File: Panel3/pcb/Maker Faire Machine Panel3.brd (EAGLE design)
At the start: 101.6 x 87.6 mm, 22 parts, among them IC1 TJA1049

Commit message: Add 2nd CAN terminal block for ease of wiring
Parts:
- added JP8: (no value), SparkFun-Connectors:SCREWTERMINAL-3.5MM-2
- renumbered JP3 to JP9
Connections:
- net CANH: now also JP8.1
- net CANL: now also JP8.2
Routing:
- net CANL: track 16.5 -> 27.3 mm
- net CANH: track 17.7 -> 28.0 mm
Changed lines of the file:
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@@
 <attribute name="PARTNO" value="12065C104KAT2A" x="62.23" y="12.7" size="1.778" layer="27" display="off"/>
 </element>
-<element name="JP3" library="SparkFun-Connectors" package="SCREWTERMINAL-3.5MM-2" value="" x="92.71" y="26.67" rot="R90">
+<element name="JP9" library="SparkFun-Connectors" package="SCREWTERMINAL-3.5MM-2" value="" x="92.71" y="26.67" rot="R90">
 <attribute name="PROD_ID" value="CONN-08399" x="92.71" y="26.67" size="1.778" layer="27" rot="R90" display="off"/>
 </element>
@@
 <element name="JP7" library="SparkFun-Connectors" package="POWER_JACK_PTH" value="POWER_JACKPTH" x="13.97" y="87.63" rot="R180">
 <attribute name="PROD_ID" value="CONN-08197" x="13.97" y="87.63" size="1.778" layer="27" rot="R180" display="off"/>
+</element>
+<element name="JP8" library="SparkFun-Connectors" package="SCREWTERMINAL-3.5MM-2" value="" x="92.71" y="16.51" rot="R90">
+<attribute name="PROD_ID" value="CONN-08399" x="92.71" y="16.51" size="1.778" layer="27" rot="R90" display="off"/>
 </element>
 </elements>
@@
 <vertex x="1.27" y="7.62"/>
 </polygon>
+<wire x1="82.61" y1="28.575" x2="77.41" y2="27.305" width="0" layer="19" extent="1-1"/>
 </signal>
 <signal name="VBAT">
@@
 <signal name="CANH">
 <contactref element="IC1" pad="7"/>
-<contactref element="JP3" pad="1"/>
+<contactref element="JP9" pad="1"/>
 <wire x1="79.375" y1="28.575" x2="77.41" y2="28.575" width="0.254" layer="1"/>
 <wire x1="79.375" y1="27.305" x2="79.375" y2="28.575" width="0.254" layer="1"/>
 <wire x1="80.645" y1="26.035" x2="79.375" y2="27.305" width="0.254" layer="1"/>
-<wire x1="92.71" y1="26.035" x2="80.645" y2="26.035" width="0.254" layer="1"/>
+<wire x1="92.71" y1="26.035" x2="90.805" y2="26.035" width="0.254" layer="1"/>
+<wire x1="90.805" y1="26.035" x2="80.645" y2="26.035" width="0.254" layer="1"/>
 <wire x1="92.71" y1="26.67" x2="92.71" y2="26.035" width="0.254" layer="1"/>
+<contactref element="JP8" pad="1"/>
+<wire x1="90.805" y1="18.415" x2="92.71" y2="16.51" width="0.254" layer="1"/>
+<wire x1="90.805" y1="26.035" x2="90.805" y2="18.415" width="0.254" layer="1"/>
 </signal>
 <signal name="CANL">
 <contactref element="IC1" pad="6"/>
-<contactref element="JP3" pad="2"/>
+<contactref element="JP9" pad="2"/>
 <wire x1="80.645" y1="29.845" x2="77.41" y2="29.845" width="0.254" layer="1"/>
 <wire x1="81.28" y1="29.21" x2="80.645" y2="29.845" width="0.254" layer="1"/>
 <wire x1="92.71" y1="29.21" x2="81.28" y2="29.21" width="0.254" layer="1"/>
-<wire x1="92.71" y1="30.17" x2="92.71" y2="29.21" width="0.254" layer="1"/>
+<contactref element="JP8" pad="2"/>
+<wire x1="94.615" y1="22.225" x2="92.71" y2="20.32" width="0.254" layer="1"/>
+<wire x1="94.615" y1="27.305" x2="94.615" y2="22.225" width="0.254" layer="1"/>
+<wire x1="92.71" y1="29.21" x2="94.615" y2="27.305" width="0.254" layer="1"/>
+<wire x1="92.71" y1="20.32" x2="92.71" y2="20.01" width="0.254" layer="1"/>
+<wire x1="92.71" y1="29.21" x2="92.71" y2="30.17" width="0.254" layer="1"/>
 </signal>
 <signal name="N$3">

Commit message: Increase cutoff frequency of ball detector lowpass
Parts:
- C1, C2: value 0.1uF -> 0.01uF
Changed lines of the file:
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@@
 </autorouter>
 <elements>
-<element name="C1" library="SparkFun-Passives" package="1206" value="0.1uF" x="82.55" y="63.5"/>
-<element name="C2" library="SparkFun-Passives" package="1206" value="0.1uF" x="82.55" y="41.91"/>
+<element name="C1" library="SparkFun-Passives" package="1206" value="0.01uF" x="82.55" y="63.5"/>
+<element name="C2" library="SparkFun-Passives" package="1206" value="0.01uF" x="82.55" y="41.91"/>
 <element name="D1" library="SparkFun-DiscreteSemi" package="SMA-DIODE" value="" x="36.83" y="74.93"/>
 <element name="JP1" library="SparkFun-Connectors" package="SCREWTERMINAL-3.5MM-4" value="" x="92.71" y="71.12" rot="R90"/>

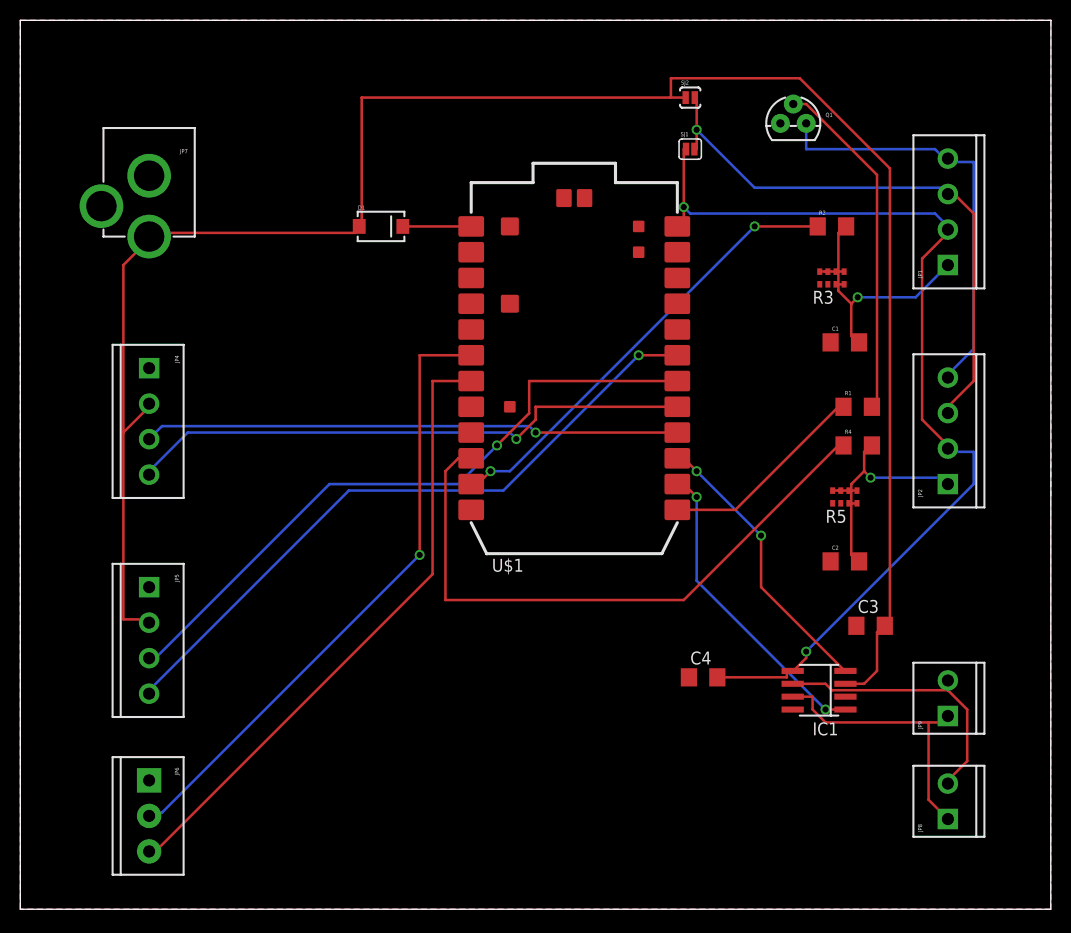
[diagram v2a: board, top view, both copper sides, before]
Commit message: Finished Panel 3 PCB Layout
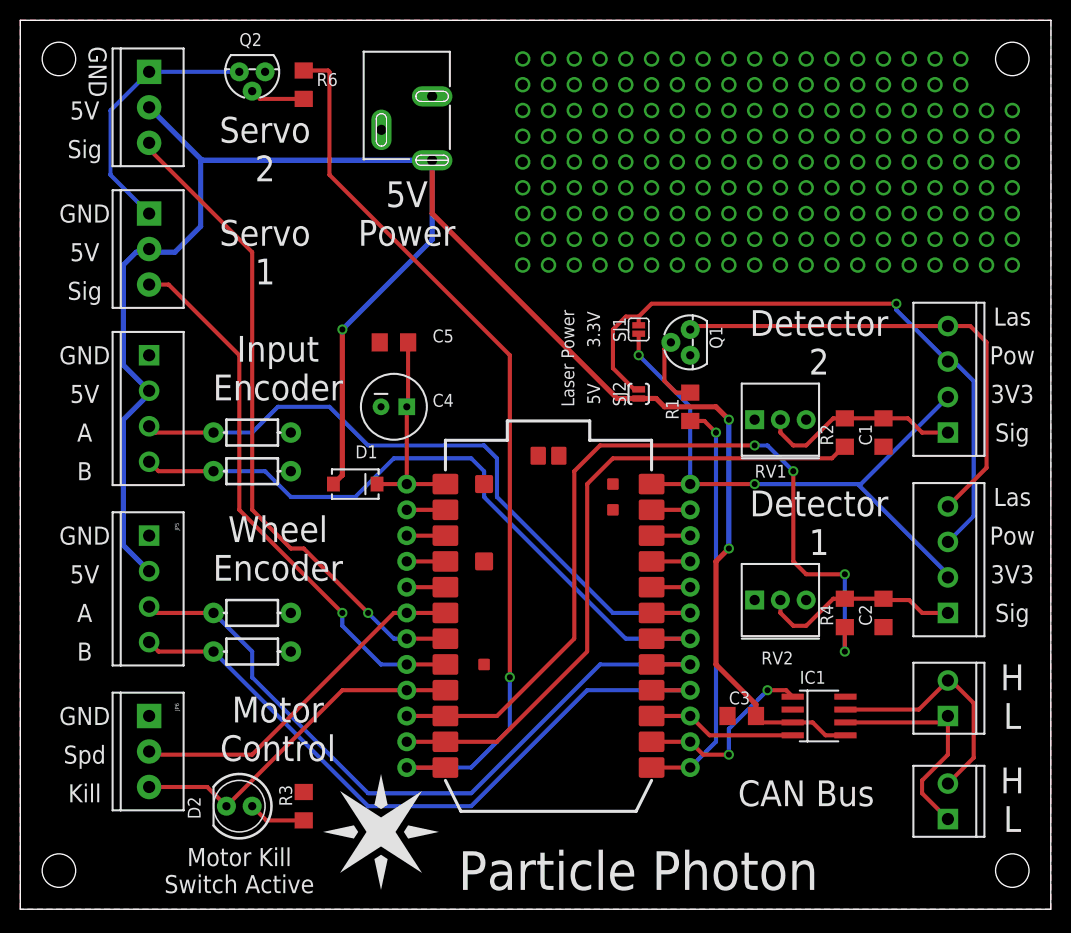
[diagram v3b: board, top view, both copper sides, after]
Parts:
- added C5: 0.1uF, SparkFun-Capacitors:1206
- added D2: (no value), SparkFun-LED:LED5MM
- added JP10, JP3: (no value), SparkFun-Connectors:SCREWTERMINAL-3.5MM-3
- added JP11, JP12: (no value), SparkFun-Connectors:1X12_NO_SILK
- added Q2: (no value), SparkFun-DiscreteSemi:TO-92
- added R6: 1k, SparkFun-Passives:1206
- added R7, R8, R9: (no value), SparkFun-Resistors:AXIAL-0.3-KIT
- added RV1, RV2: 2k, SparkFun-Electromechanical:3362U
- added STANDOFF1, STANDOFF2, STANDOFF3, STANDOFF4: STAND-OFF, SparkFun-Electromechanical:STAND-OFF
- C3: device rcl:C1206 -> SparkFun-Capacitors:1206
- C4: value 0.1u -> 100uF; device rcl:C1206 -> SparkFun-Capacitors:CPOL-RADIAL-100UF-25V
- JP7: value POWER_JACKPTH -> POWER_JACKSLT; device SparkFun-Connectors:POWER_JACK_PTH -> SparkFun-Connectors:POWER_JACK_SLOT
- R3: value 2k -> 1k; device SparkFun-Passives:0603-ARV -> SparkFun-Passives:1206
- R5: value 2k -> (none); device SparkFun-Passives:0603-ARV -> SparkFun-Resistors:AXIAL-0.3-KIT
- moved R3 73.6 mm to (29.2, 17.8), turned to 270 degrees
- moved R5 58.5 mm to (24.1, 50.8), turned to 180 degrees
- moved C4 40.5 mm to (38.1, 57.1)
- moved JP7 31.4 mm to (44.5, 95.2)
- moved SJ2 29.6 mm to (62.2, 58.4), turned to 90 degrees
- moved D1 25.5 mm to (34.3, 49.5)
- moved U$1 25.5 mm to (43.2, 16.5)
- moved Q1 23.9 mm to (67.3, 63.5), turned to 90 degrees
- moved R2 20.4 mm to (82.5, 54.6), turned to 90 degrees
- moved SJ1 18.5 mm to (62.2, 64.8), turned to 90 degrees
- moved R4 16.6 mm to (82.5, 36.8), turned to 90 degrees
- moved JP1 16.5 mm to (92.7, 54.6)
- moved R1 16.5 mm to (67.3, 57.1), turned to 90 degrees
- moved C3 15.5 mm to (72.4, 26.7)
- moved JP2 12.7 mm to (92.7, 36.8)
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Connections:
- removed net DETECTOR1: R2.1, U$1.11
- removed net DETECTOR2: R4.1, U$1.10
- removed net DETECTOR_SIG1: C1.2, JP1.1, R2.2, R3.3, R3.4, R3.5, R3.6, R3.7, R3.8
- removed net DETECTOR_SIG2: C2.2, JP2.1, R4.2, R5.3, R5.4, R5.5, R5.6, R5.7, R5.8
- removed net N$2: D1.C, U$1.1
- removed net N$3: U$1.2
- removed net VBAT: U$1.22
- new net DETECTOR_1: JP11.2, R2.1, U$1.11
- new net DETECTOR_2: JP11.3, R4.1, U$1.10
- new net DETECTOR_SIG_1: C1.2, JP1.1, R2.2, RV1.P$2
- new net DETECTOR_SIG_2: C2.2, JP2.1, R4.2, RV2.P$2
- new net N$11: JP12.8, U$1.20
- new net N$13: JP12.10, U$1.22
- new net N$14: JP12.11, U$1.23
- new net N$4: Q2.2, R6.2
- new net N$5: D2.A, R3.2
- new net RX: JP11.9, U$1.4
- new net SERVO_1: JP11.5, JP3.3, U$1.8
- new net SERVO_2: JP10.3, JP11.6, U$1.7
- new net SERVO_EN: JP11.1, R6.1, U$1.12
- new net SERVO_GND: JP10.1, JP3.1, Q2.3
- new net TX: JP11.10, U$1.3
- new net VIN: C4.1, C5.1, D1.C, JP11.12, U$1.1
- new net WKP: JP11.8, U$1.5
- net 3.3V: now also JP12.12; no longer C4.2, IC1.5
- net 5V: now also IC1.5, JP10.2, JP3.2
- net CANH: now also JP8.2, JP9.2; no longer JP8.1, JP9.1
- net CANL: now also JP8.1, JP9.1; no longer JP8.2, JP9.2
- net CANRX: now also JP12.3
- net CANTX: now also JP12.2
- net GND: now also C4.2, C5.2, JP11.11, JP12.9, JP7.GND@1, JP7.GND@2, Q2.1, R5.P$1, R7.P$1, R8.P$1, R9.P$1, RV1.P$1, RV2.P$1, U$1.2; no longer C4.1, JP7.GND, JP7.GNDBREAK, R5.1
- net INPUT_ENCODER_A: now also JP12.7, R7.P$2, U$1.19; no longer U$1.16
- net INPUT_ENCODER_B: now also JP12.6, R5.P$2, U$1.18; no longer U$1.17
- net LASER_EN: now also JP12.1
- net MOTOR_KILL: now also D2.K, JP11.4, U$1.9; no longer U$1.7
- net MOTOR_SPEED: now also JP11.7
- net WHEEL_ENCODER_A: now also JP12.5, R9.P$2, U$1.17; no longer U$1.18
- net WHEEL_ENCODER_B: now also JP12.4, R8.P$2, U$1.16; no longer U$1.19
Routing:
- net SERVO_EN: track 0.00 -> 90.3 mm, vias 0 -> 1
- net DETECTOR_2: track 0.00 -> 84.4 mm, vias 0 -> 4
- net DETECTOR_1: track 0.00 -> 65.1 mm
- net SERVO_2: track 0.00 -> 64.7 mm, vias 0 -> 1
- net DETECTOR2: track 61.3 -> 0.00 mm
- net SERVO_1: track 0.00 -> 54.4 mm, vias 0 -> 1
- net DETECTOR1: track 44.7 -> 0.00 mm, vias 2 -> 0
- net 3.3V: track 98.9 -> 62.6 mm, vias 2 -> 3
- net 5V: track 193.4 -> 222.1 mm, vias 0 -> 3
- net MOTOR_KILL: track 63.0 -> 34.7 mm
- net DETECTOR_SIG1: track 27.9 -> 0.00 mm, vias 1 -> 0
- net N$1: track 34.5 -> 7.09 mm
- net MOTOR_SPEED: track 62.3 -> 35.1 mm, vias 1 -> 0
- net SERVO_GND: track 0.00 -> 26.0 mm
- net DETECTOR_SIG2: track 25.6 -> 0.00 mm, vias 1 -> 0
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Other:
- board text added: "3.3V"
- board text added: "3V3"
- board text added: "5V"
- board text added: "5V Power"
- board text added: "A"
- board text added: "B"
- board text added: "CAN Bus"
- board text added: "Detector 1"
- board text added: "Detector 2"
- board text added: "GND"
- board text added: "H"
- board text added: "Input Encoder"
- board text added: "Kill"
- board text added: "L"
- board text added: "Las"
- board text added: "Laser Power"
- board text added: "Motor Control"
- board text added: "Motor Kill Switch Active"
- board text added: "Particle Photon"
- board text added: "Pow"
- board text added: "Servo 1"
- board text added: "Servo 2"
- board text added: "Sig"
- board text added: "Spd"
- board text added: "Wheel Encoder"
